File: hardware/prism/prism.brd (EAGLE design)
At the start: 100 x 79 mm, 174 parts, among them IC1 XMEGA128-A1, IC2 74LVC4245APW, IC3 LM2731XMF, IC4 74LVC4245APW, IC5 LM25011MY, IC6 NCV78M05BDTRKG, IC7 NRF24L01+, IC8 MAX3232CSE, T1 MMBT2222LT1G, T2 NTGS4111PT1G, T3 MMBT2222LT1G, T4 MMBT2222LT1G, T5 NTGS4111PT1G, T6 MMBT2222LT1G, T7 MMBT2222LT1G, T8 NTGS4111PT1G

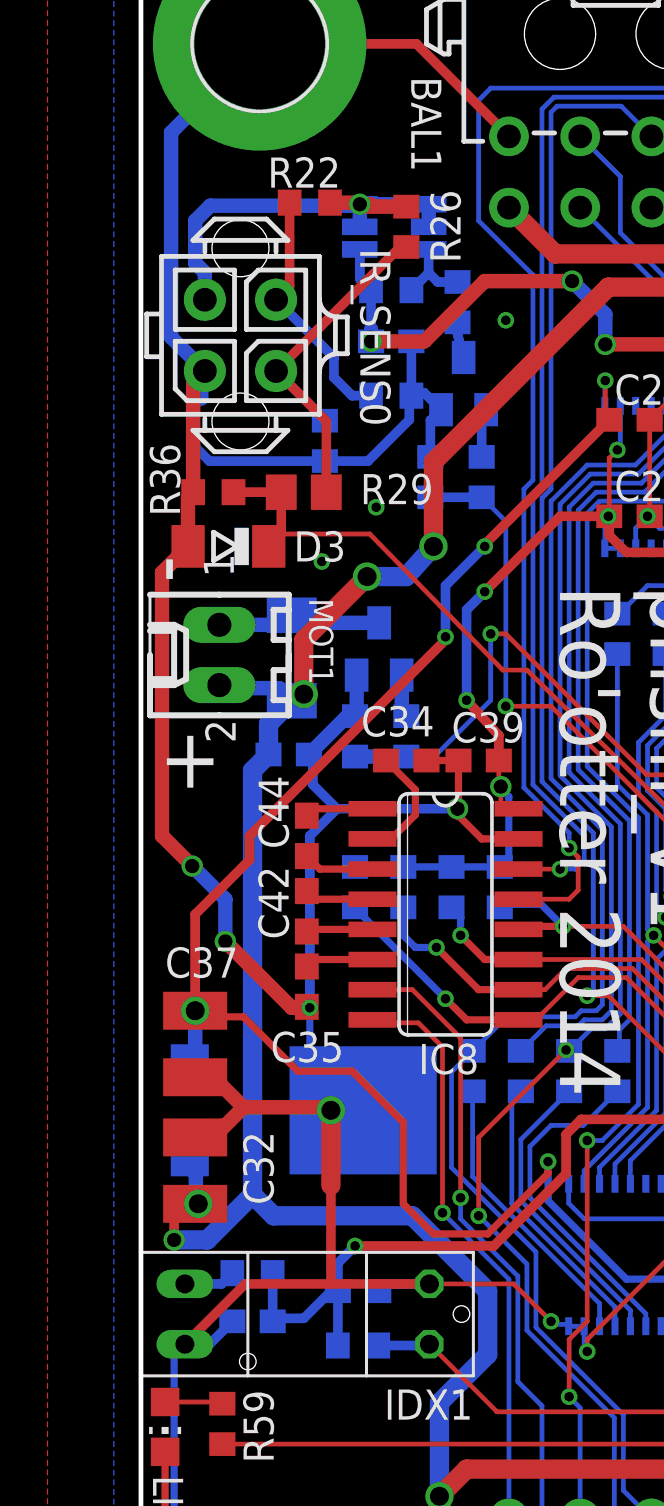
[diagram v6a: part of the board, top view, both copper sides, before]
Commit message: ir index polarization resistor value changed after Damien review of prism_idx_suport board
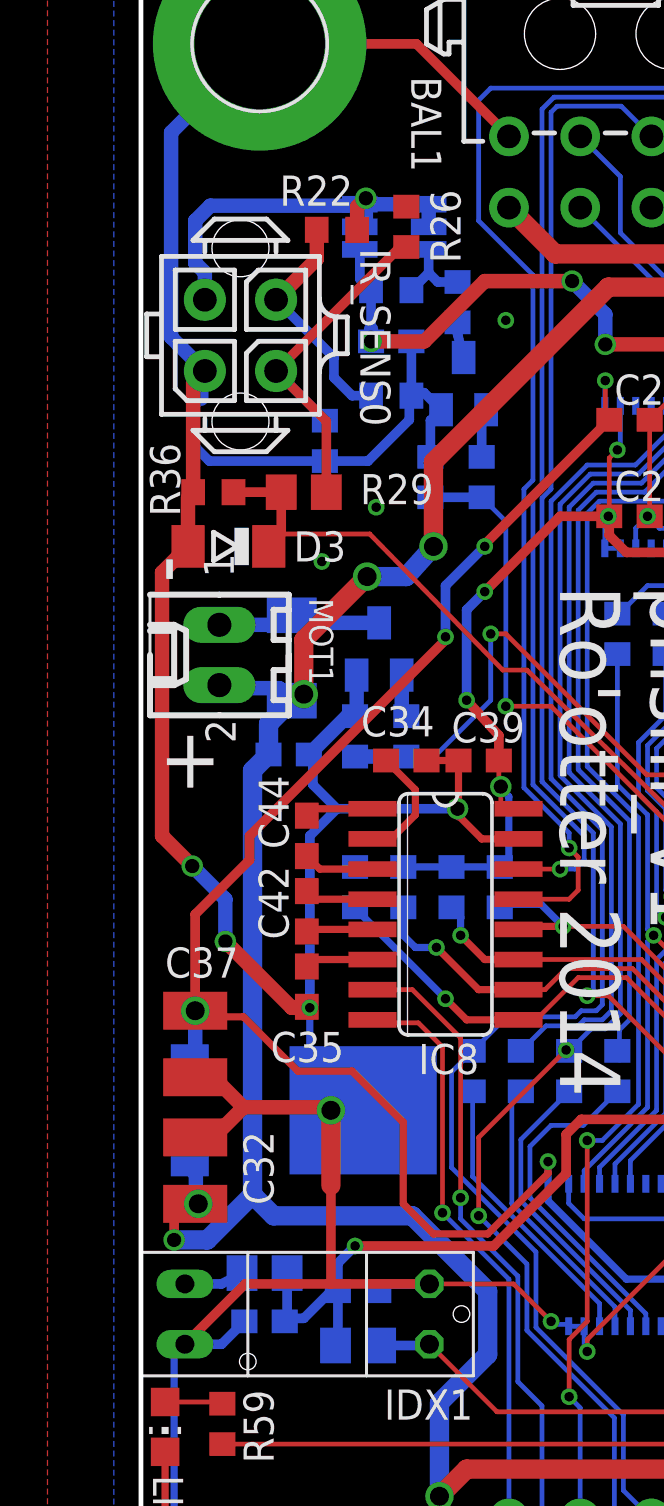
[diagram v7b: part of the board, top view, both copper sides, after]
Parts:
- R17: value 270-F -> 100-E; device robotter_resistor:R0603 -> robotter_resistor:R0805
- R24: value 4K7-F -> 270-E; device robotter_resistor:R0603 -> robotter_resistor:R0805
- moved R22 1.62 mm to (8.26, 66.2)
- moved C5 0.51 mm to (5.21, 20.2)
- moved R17 0.51 mm to (5.21, 22.2)
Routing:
- net N$58: track 19.4 -> 17.7 mm
- net N$41: track 10.5 -> 9.82 mm
- net +3V3: track 398.7 -> 398.1 mm
- net GND: track 811.7 -> 812.2 mm
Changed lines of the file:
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@@
 <layer number="37" name="tTest" color="7" fill="1" visible="no" active="yes"/>
 <layer number="38" name="bTest" color="7" fill="1" visible="no" active="yes"/>
-<layer number="39" name="tKeepout" color="4" fill="11" visible="no" active="yes"/>
-<layer number="40" name="bKeepout" color="1" fill="11" visible="no" active="yes"/>
+<layer number="39" name="tKeepout" color="4" fill="11" visible="yes" active="yes"/>
+<layer number="40" name="bKeepout" color="1" fill="11" visible="yes" active="yes"/>
 <layer number="41" name="tRestrict" color="4" fill="10" visible="no" active="yes"/>
 <layer number="42" name="bRestrict" color="1" fill="10" visible="no" active="yes"/>
@@
 <attribute name="VALUE" x="46.482" y="41.402" size="1.27" layer="27" rot="R270"/>
 </element>
-<element name="C5" library="robotter_capacitor" package="C0603" value="100nF 50V" x="4.699" y="20.193" smashed="yes" rot="MR0">
-<attribute name="RS" value=" 723-5534 " x="4.699" y="20.193" size="1.778" layer="28" rot="MR0" display="off"/>
-<attribute name="NAME" x="5.207" y="17.272" size="1.27" layer="26" rot="MR90"/>
-<attribute name="VALUE" x="5.334" y="18.288" size="1.27" layer="28" rot="MR0"/>
+<element name="C5" library="robotter_capacitor" package="C0603" value="100nF 50V" x="5.207" y="20.193" smashed="yes" rot="MR0">
+<attribute name="RS" value=" 723-5534 " x="5.207" y="20.193" size="1.778" layer="28" rot="MR0" display="off"/>
+<attribute name="NAME" x="5.715" y="17.272" size="1.27" layer="26" rot="MR90"/>
+<attribute name="VALUE" x="5.842" y="18.288" size="1.27" layer="28" rot="MR0"/>
 </element>
 <element name="C3" library="robotter_capacitor" package="C0603" value="100nF 50V" x="94.996" y="9.017" smashed="yes" rot="MR270">
@@
 <attribute name="VALUE" x="8.509" y="23.368" size="1.27" layer="28" rot="MR180"/>
 </element>
-<element name="R24" library="robotter_resistor" package="R0603" value="4K7-F" x="9.144" y="19.177" smashed="yes" rot="MR0">
-<attribute name="RS" value="740-8959" x="9.144" y="19.177" size="1.778" layer="28" rot="MR0" display="off"/>
+<element name="R24" library="robotter_resistor" package="R0805" value="270-E" x="9.144" y="19.177" smashed="yes" rot="MR0">
+<attribute name="RS" value="740-9019" x="9.144" y="19.177" size="1.778" layer="28" rot="MR0" display="off"/>
 <attribute name="NAME" x="10.922" y="17.018" size="1.27" layer="26" rot="MR0"/>
 <attribute name="VALUE" x="9.779" y="17.272" size="1.27" layer="28" rot="MR0"/>
 </element>
-<element name="R17" library="robotter_resistor" package="R0603" value="270-F" x="4.699" y="22.225" smashed="yes" rot="MR180">
-<attribute name="RS" value=" 679-0071" x="4.699" y="22.225" size="1.778" layer="28" rot="MR180" display="off"/>
-<attribute name="NAME" x="5.08" y="22.987" size="1.27" layer="26" rot="MR0"/>
-<attribute name="VALUE" x="4.064" y="24.13" size="1.27" layer="28" rot="MR180"/>
+<element name="R17" library="robotter_resistor" package="R0805" value="100-E" x="5.207" y="22.225" smashed="yes" rot="MR180">
+<attribute name="RS" value="223-0297" x="5.207" y="22.225" size="1.778" layer="28" rot="MR180" display="off"/>
+<attribute name="NAME" x="6.604" y="23.114" size="1.27" layer="26" rot="MR0"/>
+<attribute name="VALUE" value="100-E" x="4.572" y="24.13" size="1.27" layer="28" rot="MR180"/>
 </element>
 <element name="C18" library="robotter_capacitor" package="C0603" value="100nF 50V" x="94.234" y="58.547" smashed="yes" rot="R270">
@@
 <attribute name="VALUE" x="8.691" y="64.722" size="1.27" layer="27" rot="R270"/>
 </element>
-<element name="R22" library="robotter_resistor" package="R0603" value="0-F" x="7.112" y="67.31" smashed="yes">
-<attribute name="NAME" x="5.334" y="67.945" size="1.27" layer="25"/>
-<attribute name="VALUE" x="6.477" y="65.405" size="1.27" layer="27"/>
+<element name="R22" library="robotter_resistor" package="R0603" value="0-F" x="8.255" y="66.167" smashed="yes">
+<attribute name="NAME" x="5.842" y="67.183" size="1.27" layer="25"/>
+<attribute name="VALUE" x="7.62" y="64.262" size="1.27" layer="27"/>
 </element>
 <element name="R23" library="robotter_resistor" package="R0603" value="0-F" x="10.541" y="59.182" smashed="yes" rot="MR0">
@@
 <wire x1="4.39" y1="21.77" x2="8.001" y2="21.77" width="0.4064" layer="1"/>
 <wire x1="8.001" y1="21.77" x2="12.15" y2="21.77" width="0.4064" layer="1"/>
-<wire x1="3.849" y1="20.193" x2="2.886" y2="19.23" width="0.4064" layer="16"/>
-<wire x1="2.886" y1="19.23" x2="1.85" y2="19.23" width="0.4064" layer="16"/>
 <wire x1="8.001" y1="25.919" x2="8.001" y2="21.77" width="0.4064" layer="1"/>
 <wire x1="25.019" y1="21.551" x2="25.82" y2="22.352" width="0.4064" layer="16"/>
@@
 <via x="15.367" y="62.357" extent="1-16" drill="0.4" shape="octagon"/>
 <wire x1="85.471" y1="6.438" x2="85.471" y2="7.747" width="0.4064" layer="16"/>
+<wire x1="4.357" y1="20.193" x2="3.394" y2="19.23" width="0.4064" layer="16"/>
+<wire x1="3.394" y1="19.23" x2="1.85" y2="19.23" width="0.4064" layer="16"/>
 </signal>
 <signal name="+3V3">
@@
 <contactref element="IC7" pad="2"/>
 <contactref element="R67" pad="2"/>
-<wire x1="5.549" y1="20.193" x2="5.549" y2="22.225" width="0.4064" layer="16"/>
-<wire x1="8.167" y1="18.923" x2="8.294" y2="19.177" width="0.4064" layer="16"/>
+<wire x1="8.167" y1="18.923" x2="8.194" y2="19.177" width="0.4064" layer="16"/>
 <wire x1="8.294" y1="21.463" x2="8.001" y2="21.463" width="0.4064" layer="16"/>
 <wire x1="8.001" y1="21.463" x2="6.858" y2="20.32" width="0.4064" layer="16"/>
-<wire x1="6.858" y1="20.32" x2="5.676" y2="20.32" width="0.4064" layer="16"/>
-<wire x1="5.676" y1="20.32" x2="5.549" y2="20.193" width="0.4064" layer="16"/>
-<wire x1="8.294" y1="19.177" x2="8.294" y2="21.463" width="0.4064" layer="16"/>
 <contactref element="IDX0" pad="2"/>
 <wire x1="82.003" y1="66.548" x2="85.598" y2="66.548" width="0.3048" layer="16"/>
@@
 <wire x1="19.724" y1="53.301" x2="20.447" y2="52.578" width="0.4064" layer="1"/>
 <wire x1="17.653" y1="54.102" x2="19.724" y2="54.102" width="0.4064" layer="1"/>
+<wire x1="6.858" y1="20.32" x2="6.157" y2="20.32" width="0.4064" layer="16"/>
+<wire x1="6.057" y1="20.32" x2="6.057" y2="20.193" width="0.4064" layer="16"/>
+<wire x1="6.057" y1="20.32" x2="6.157" y2="20.32" width="0.4064" layer="16"/>
+<wire x1="6.157" y1="20.32" x2="6.157" y2="22.225" width="0.4064" layer="16"/>
+<wire x1="8.194" y1="19.177" x2="8.294" y2="19.277" width="0.4064" layer="16"/>
+<wire x1="8.294" y1="19.277" x2="8.294" y2="21.463" width="0.4064" layer="16"/>
 </signal>
 <signal name="/RESET_3V3">
@@
 <contactref element="IDX1" pad="LED_A"/>
 <contactref element="R17" pad="1"/>
-<wire x1="3.849" y1="22.225" x2="3.394" y2="21.77" width="0.4064" layer="16"/>
+<wire x1="4.257" y1="22.225" x2="3.394" y2="21.77" width="0.4064" layer="16"/>
 <wire x1="3.394" y1="21.77" x2="1.85" y2="21.77" width="0.4064" layer="16"/>
 </signal>
@@
 <contactref element="IDX1" pad="TRANSISTOR_C"/>
 <contactref element="R24" pad="1"/>
-<wire x1="9.994" y1="19.177" x2="12.097" y2="19.177" width="0.4064" layer="16"/>
+<wire x1="10.094" y1="19.177" x2="12.097" y2="19.177" width="0.4064" layer="16"/>
 <wire x1="12.097" y1="19.177" x2="12.15" y2="19.23" width="0.4064" layer="16"/>
 <wire x1="12.15" y1="19.23" x2="14.997" y2="16.383" width="0.2" layer="1"/>
@@
 <wire x1="8.128" y1="59.944" x2="8.128" y2="60.785" width="0.4064" layer="16"/>
 <wire x1="8.128" y1="60.785" x2="5.691" y2="63.222" width="0.4064" layer="16"/>
-<wire x1="6.262" y1="67.31" x2="6.262" y2="63.793" width="0.4064" layer="1"/>
-<wire x1="6.262" y1="63.793" x2="5.691" y2="63.222" width="0.4064" layer="1"/>
+<wire x1="7.405" y1="66.167" x2="7.405" y2="64.936" width="0.6096" layer="1"/>
+<wire x1="7.405" y1="64.936" x2="5.691" y2="63.222" width="0.6096" layer="1"/>
 </signal>
 <signal name="N$8">
@@
 <contactref element="R26" pad="2"/>
 <contactref element="R22" pad="2"/>
-<wire x1="9.218" y1="66.294" x2="9.218" y2="67.244" width="0.6096" layer="16"/>
-<wire x1="9.218" y1="67.244" x2="9.157" y2="67.183" width="0.6096" layer="16"/>
 <wire x1="9.157" y1="67.183" x2="2.921" y2="67.183" width="0.6096" layer="16"/>
 <wire x1="2.921" y1="67.183" x2="2.286" y2="66.548" width="0.6096" layer="16"/>
@@
 <wire x1="2.286" y1="64.77" x2="2.691" y2="64.365" width="0.6096" layer="16"/>
 <wire x1="2.691" y1="64.365" x2="2.691" y2="63.222" width="0.6096" layer="16"/>
-<wire x1="9.218" y1="67.244" x2="12.118" y2="67.244" width="0.6096" layer="16"/>
 <wire x1="12.118" y1="67.244" x2="12.118" y2="66.294" width="0.6096" layer="16"/>
-<via x="9.218" y="67.244" extent="1-16" drill="0.6" shape="octagon"/>
-<wire x1="9.679" y1="67.244" x2="9.218" y2="67.244" width="0.6096" layer="1"/>
-<wire x1="11.176" y1="67.144" x2="9.218" y2="67.144" width="0.6096" layer="1"/>
-<wire x1="9.218" y1="67.144" x2="9.218" y2="67.244" width="0.6096" layer="1"/>
-<wire x1="7.962" y1="67.31" x2="9.218" y2="67.31" width="0.6096" layer="1"/>
-<wire x1="9.218" y1="67.31" x2="9.218" y2="67.244" width="0.6096" layer="1"/>
+<via x="9.472" y="67.498" extent="1-16" drill="0.6" shape="octagon"/>
+<wire x1="12.118" y1="67.244" x2="9.218" y2="67.244" width="0.6096" layer="16"/>
+<wire x1="9.157" y1="67.183" x2="9.218" y2="67.244" width="0.6096" layer="16"/>
+<wire x1="9.472" y1="67.498" x2="9.218" y2="67.244" width="0.6096" layer="16"/>
+<wire x1="9.218" y1="66.294" x2="9.472" y2="66.548" width="0.6096" layer="16"/>
+<wire x1="9.472" y1="66.548" x2="9.472" y2="67.498" width="0.6096" layer="16"/>
+<wire x1="9.105" y1="66.167" x2="9.105" y2="67.131" width="0.6096" layer="1"/>
+<wire x1="9.105" y1="67.131" x2="9.472" y2="67.498" width="0.6096" layer="1"/>
+<wire x1="12.118" y1="67.244" x2="11.176" y2="67.144" width="0" layer="19" extent="1-16"/>
 </signal>
 <signal name="BEACON_ID_0_3V3">

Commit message: board update after Damien review
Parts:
- moved R55 2.67 mm to (40.0, 70.2)
- moved R51 2.43 mm to (40.0, 66.7)
- moved R54 1.91 mm to (37.2, 71.5)
- moved T7 1.78 mm to (37.1, 68.5)
- moved R46 1.65 mm to (37.0, 65.4)
- moved T8 0.65 mm to (37.2, 75.7), turned to 0 degrees
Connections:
- net GND: now also IC5.THERMAL
- net SYNC_IN_0_3V3: now also IC1.37; no longer IC1.27
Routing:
- net VBAT: track 338.3 -> 344.9 mm, vias 13 -> 26
- net N$30: track 7.52 -> 13.5 mm
- net SYNC_IN_0_3V3: track 16.5 -> 22.1 mm
- net ON/OFF_SENSOR_1_3V1: track 13.6 -> 11.3 mm
- net N$58: track 17.7 -> 19.6 mm
- net GND: track 812.2 -> 810.6 mm, vias 57 -> 65
- net N$26: track 4.33 -> 5.88 mm
- net SYNC_IN_1_3V3: track 18.0 -> 17.4 mm
- net LOW_BAT_LED_3V3: track 56.7 -> 57.2 mm
- net N$25: track 2.56 -> 2.04 mm
